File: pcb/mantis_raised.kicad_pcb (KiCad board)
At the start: 2 copper layers, 131 x 90.3 mm, 42 parts

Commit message: pcb: New Raised PCB with LEDs
Generated with Ergogen, updated with connect_leds.awk, footprints
updated and traces routed with kicad.

Signed-off-by: Felix Kuehling <felix.kuehling@gmail.com>
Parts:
- removed ? (x5): MountingHole_2.2mm_M2_Pad, MountingHole:MountingHole_2.2mm_M2_Pad
- removed ? (x4): PinHeader_1x02_P2.54mm_Vertical, Connector_PinHeader_2.54mm:PinHeader_1x02_P2.54mm_Vertical
- removed ?: PinHeader_1x05_P2.54mm_Vertical, Connector_PinHeader_2.54mm:PinHeader_1x05_P2.54mm_Vertical
- added B1: , E73:SW_TACT_ALPS_SKQGABE010, F.Cu at (254.0, 67.3)
- added LED1: , WS2812B, F.Cu at (235.1, 87.4)
- added LED10: , WS2812B, F.Cu at (262.2, 106.0)
- added LED11: , WS2812B, F.Cu at (283.7, 110.7)
- added LED12: , WS2812B, F.Cu at (272.9, 129.3)
- added LED13: , WS2812B, F.Cu at (298.5, 131.7)
- added LED14: , WS2812B, F.Cu at (262.2, 146.7)
- added LED15: , WS2812B, F.Cu at (313.3, 146.7)
- added LED16: , WS2812B, F.Cu at (287.8, 144.4)
- added LED2: , WS2812B, F.Cu at (245.8, 106.0)
- added LED3: , WS2812B, F.Cu at (224.3, 110.7)
- added LED4: , WS2812B, F.Cu at (235.1, 129.3)
- added LED5: , WS2812B, F.Cu at (209.5, 131.7)
- added LED6: , WS2812B, F.Cu at (245.8, 146.7)
- added LED7: , WS2812B, F.Cu at (194.7, 146.7)
- added LED8: , WS2812B, F.Cu at (220.2, 144.4)
- added LED9: , WS2812B, F.Cu at (272.9, 87.4)
- added MCU1: , ProMicro, F.Cu at (254.0, 78.1)
- added MCU2: , ProMicro, F.Cu at (254.0, 126.4)
- added PAD1: , SMDPad, F.Cu at (206.8, 160.4)
- added PAD2: , SMDPad, F.Cu at (250.0, 139.4)
- added PAD3: , SMDPad, F.Cu at (239.1, 75.8)
- added PAD4: , SMDPad, F.Cu at (301.2, 160.4)
- added PAD5: , SMDPad, F.Cu at (258.0, 139.4)
- added PAD6: , SMDPad, F.Cu at (268.9, 75.8)
- moved S6 169.9 mm to (241.8, 149.1), turned to 120 degrees
- moved S13 161.8 mm to (298.5, 127.0), turned to -360 degrees
- moved D6 158.8 mm to (238.7, 150.8), turned to -60 degrees
- moved D13 152.2 mm to (298.5, 123.5), turned to -180 degrees
- moved S2 149.0 mm to (241.8, 108.4), turned to 120 degrees
- moved S15 148.9 mm to (309.2, 149.1), turned to -240 degrees
- moved S16 148.9 mm to (287.8, 149.1)
- moved S1 145.0 mm to (231.0, 89.8), turned to 120 degrees
- moved S12 144.3 mm to (277.0, 127.0), turned to -60 degrees
- moved D16 141.3 mm to (287.8, 152.6), turned to 0 degrees
- moved D12 138.2 mm to (280.0, 125.2), turned to 120 degrees
- moved D2 138.0 mm to (238.7, 110.1), turned to -60 degrees
- moved D15 137.9 mm to (306.2, 150.8), turned to -60 degrees
- moved S11 135.1 mm to (287.8, 108.4), turned to -60 degrees
- moved D1 133.5 mm to (228.0, 91.5), turned to -60 degrees
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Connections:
- D1 pad 1: P2 -> R3
- D1 pad 2: c4_r1 -> c4_r3
- D10 pad 1: P0 -> R3
- D10 pad 2: c4m_r2 -> mirror_c5_r3
- D11 pad 1: P2 -> R2
- D11 pad 2: c5m_r1 -> mirror_c4_r2
- D12 pad 1: P0 -> R2
- D12 pad 2: c5m_r2 -> mirror_c5_r2
- D13 pad 1: P1 -> R1
- D13 pad 2: c5m_r3 -> mirror_c4_r1
- D14 pad 1: P3 -> R1
- D14 pad 2: c2m_rt -> mirror_c5_r1
- D15 pad 1: P3 -> RT
- D15 pad 2: c3m_rt -> mirror_c4_rt
- D16 pad 1: P3 -> RT
- D16 pad 2: c5m_rt -> mirror_c5_rt
- D2 pad 1: P0 -> R3
- D2 pad 2: c4_r2 -> c5_r3
- D3 pad 1: P2 -> R2
- D3 pad 2: c5_r1 -> c4_r2
- D4 pad 1: P0 -> R2
- D5 pad 1: P1 -> R1
- D5 pad 2: c5_r3 -> c4_r1
- D6 pad 1: P3 -> R1
- D6 pad 2: c2_rt -> c5_r1
- D7 pad 1: P3 -> RT
- D7 pad 2: c3_rt -> c4_rt
- D8 pad 1: P3 -> RT
- D9 pad 1: P2 -> R3
- D9 pad 2: c4m_r1 -> mirror_c4_r3
- S1 pad 1: c4_r1 -> C4
- S1 pad 2: P14 -> c4_r3
- S10 pad 1: c4m_r2 -> M_C5
- S10 pad 2: P7 -> mirror_c5_r3
- S11 pad 1: c5m_r1 -> M_C4
- S11 pad 2: P8 -> mirror_c4_r2
- S12 pad 1: c5m_r2 -> M_C5
- S12 pad 2: P8 -> mirror_c5_r2
- S13 pad 1: c5m_r3 -> M_C4
- S13 pad 2: P8 -> mirror_c4_r1
- S14 pad 1: c2m_rt -> M_C5
- S14 pad 2: P5 -> mirror_c5_r1
- S15 pad 1: c3m_rt -> M_C4
- S15 pad 2: P6 -> mirror_c4_rt
- S16 pad 1: c5m_rt -> M_C5
- S16 pad 2: P8 -> mirror_c5_rt
- S2 pad 1: c4_r2 -> C5
- S2 pad 2: P14 -> c5_r3
- S3 pad 1: c5_r1 -> C4
- S3 pad 2: P16 -> c4_r2
- S4 pad 1: c5_r2 -> C5
- S4 pad 2: P16 -> c5_r2
- S5 pad 1: c5_r3 -> C4
- S5 pad 2: P16 -> c4_r1
- S6 pad 1: c2_rt -> C5
- S6 pad 2: P18 -> c5_r1
- S7 pad 1: c3_rt -> C4
- S7 pad 2: P15 -> c4_rt
- S8 pad 1: c5_rt -> C5
- S8 pad 2: P16 -> c5_rt
- S9 pad 1: c4m_r1 -> M_C4
- S9 pad 2: P7 -> mirror_c4_r3
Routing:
- net P3: track 154.3 -> 0.00 mm
- net P0: track 118.5 -> 0.00 mm
- net P1: track 108.2 -> 0.00 mm
- net P2: track 107.9 -> 0.00 mm
- net P8: track 93.1 -> 0.00 mm
- net P16: track 74.3 -> 0.00 mm
- net P14: track 47.5 -> 0.00 mm
- net P7: track 35.1 -> 0.00 mm
- net P6: track 24.2 -> 0.00 mm
- net P18: track 23.6 -> 0.00 mm
- net P15: track 11.6 -> 0.00 mm
- net P5: track 11.4 -> 0.00 mm
- net c5m_rt: track 10.0 -> 0.00 mm
- net c5m_r3: track 10.0 -> 0.00 mm
- net c5m_r2: track 10.0 -> 0.00 mm
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- removed copper zone on B.Cu, net GND
- removed copper zone on F.Cu, net GND
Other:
- board size 131 x 90.3 mm -> 131.5 x 107.5 mm
- net class Default added: clearance 0.2, trace_width 0.25, via_dia 0.8, via_drill 0.4
- rule pad_to_mask_clearance: 0 -> 0.05
- board text removed: "Mantis v0.2 Felix Kühling March 2023"

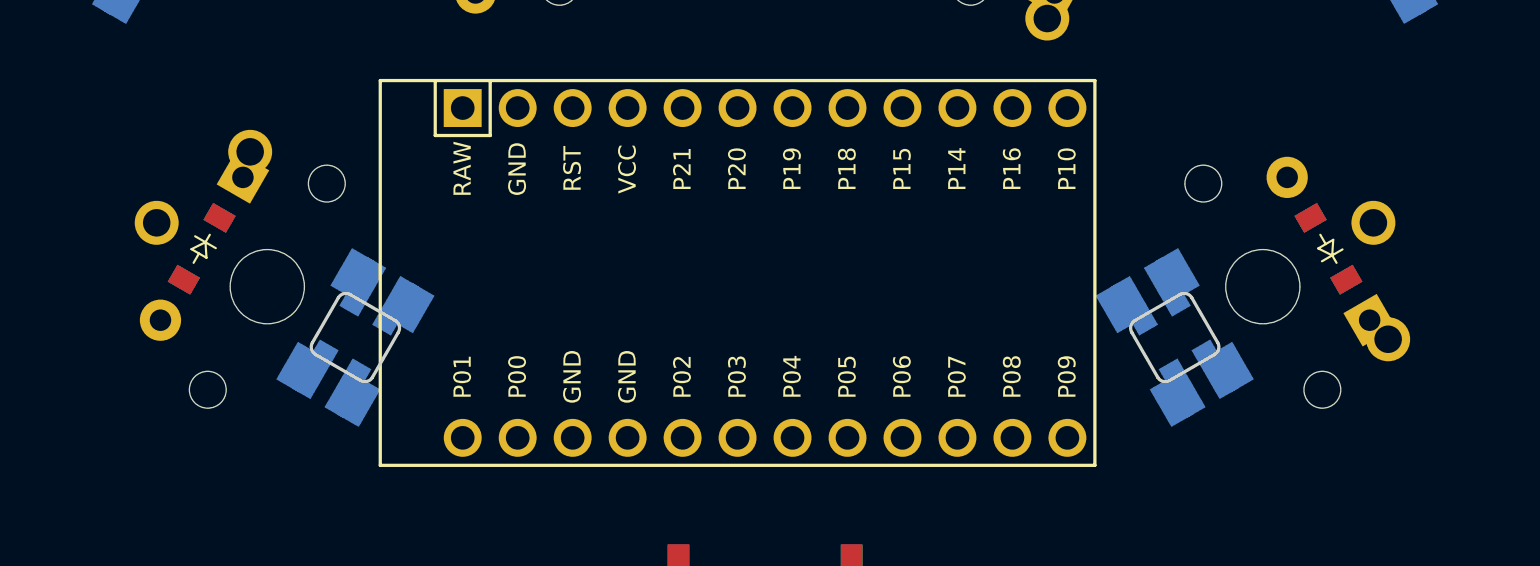
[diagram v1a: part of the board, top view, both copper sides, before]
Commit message: pcb: Update raised PCB for v0.3.3
Changes since v0.3:
- Rotated inner bottom index finger keys
- Use RAW pin for LED power supply
- Added optional level shifter on LED data pin to support 3.3V controllers
  (Using two channels on a 6 channel inverter that's available on
  AdaFruit, cheap enough and simpler than building something from
  discrete resistor and transistor)
- Added jumper to bypass level shifter for 5V controllers
- Moved ProMicro pin labels on silkscreen to the outside to make room for
  level shifter
- Slightly increased silkscreen line widths on the mantis logo/headers
- Fixed unused pad number on header footprint
- Cleaned up some routing, removed two GND vias

Signed-off-by: Felix Kuehling <felix.kuehling@gmail.com>
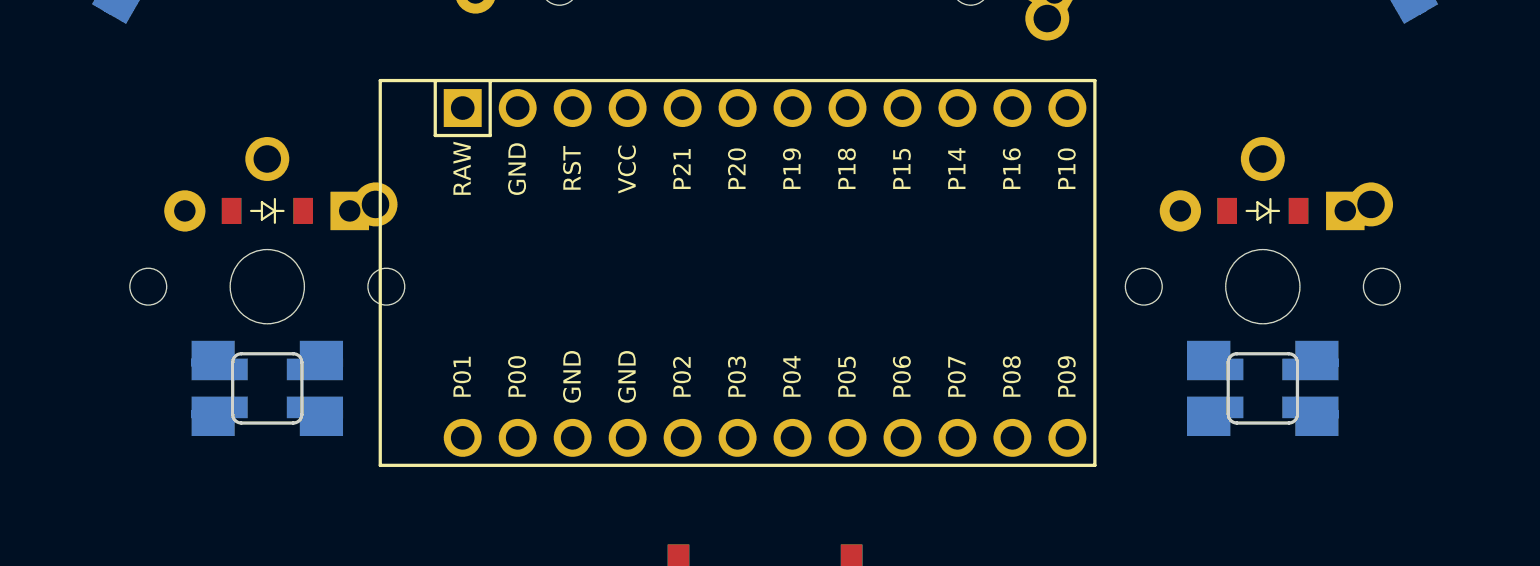
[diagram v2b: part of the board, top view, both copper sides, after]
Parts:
- moved LED12 4.70 mm to (277.0, 131.7), turned to -180 degrees
- moved LED4 4.70 mm to (231.0, 131.7), turned to 180 degrees
- moved D12 3.50 mm to (277.0, 123.5), turned to -180 degrees
- moved D4 3.50 mm to (231.0, 123.5), turned to 180 degrees
- turned S12 to -360 degrees
- turned S4 to 360 degrees
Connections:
- MCU1 pad 1: RAW -> VCC
- MCU1 pad 24: di_c4_r3 -> LED
- MCU1 pad 4: VCC -> 3_3V
- MCU2 pad 12: P10 -> di_mirror_c3_r3
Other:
- outline, holes or cut-outs redrawn
